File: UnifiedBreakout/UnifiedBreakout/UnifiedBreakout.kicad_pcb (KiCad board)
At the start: 2 copper layers, 15 parts, among them J1 MESA P3, J10 LIM Z, J11 ENCODER OUT, J12 PENDANT, J2 MESA P2, J3 ENCODER IN, J4 LIM X, J5 MOT X, J6 MOT Y, J7 ATX-24, J8 MOT Z, J9 LIM Y, K1 MOTOR POWER, K2 MIST, K3 DRAWBAR

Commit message: Unified breakout schematic "done"
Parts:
- removed K1: MOTOR POWER, Relay_THT:Relay_DPDT_Finder_40.52
- removed K2: MIST, Relay_THT:Relay_DPDT_Finder_40.52
- removed K3: DRAWBAR, Relay_THT:Relay_DPDT_Finder_40.52
- added C1: 100n, Capacitor_THT:C_Rect_L7.0mm_W2.0mm_P5.00mm, F.Cu at (149.4, 68.6)
- added C2: 100uF, Capacitor_THT:CP_Radial_D6.3mm_P2.50mm, F.Cu at (166.9, 62.7)
- added C3: 100n, Capacitor_THT:C_Rect_L7.0mm_W2.0mm_P5.00mm, F.Cu at (166.2, 46.5)
- added C4: 100uF, Capacitor_THT:CP_Radial_D6.3mm_P2.50mm, F.Cu at (158.9, 67.2)
- added C5: 100n, Capacitor_THT:C_Rect_L7.0mm_W2.0mm_P5.00mm, F.Cu at (166.2, 50.0)
- added C6: 100uF, Capacitor_THT:CP_Radial_D6.3mm_P2.50mm, F.Cu at (190.7, 44.2)
- added C7: 100n, Capacitor_THT:C_Rect_L7.0mm_W2.0mm_P5.00mm, F.Cu at (149.4, 65.0)
- added C8: 100uF, Capacitor_THT:CP_Radial_D6.3mm_P2.50mm, F.Cu at (177.0, 58.7)
- added D1: MESA P3 PWR, LED_THT:LED_D3.0mm, F.Cu at (189.6, 50.9)
- added D10: 1N4001, Diode_THT:D_DO-41_SOD81_P10.16mm_Horizontal, F.Cu at (178.1, 90.8)
- added D2: MESA P2 PWR, LED_THT:LED_D3.0mm, F.Cu at (173.8, 65.4)
- added D3: ATX PWR GOOD, LED_THT:LED_D3.0mm, F.Cu at (192.4, 35.9)
- added D4: ATX STBY, LED_THT:LED_D3.0mm, F.Cu at (192.4, 30.4)
- added D5: LED, LED_THT:LED_D3.0mm, F.Cu at (62.7, 177.5)
- added D6: 1N4001, Diode_THT:D_DO-41_SOD81_P10.16mm_Horizontal, F.Cu at (35.6, 176.9)
- added D7: LED, LED_THT:LED_D3.0mm, F.Cu at (121.2, 143.2)
- added D8: 1N4001, Diode_THT:D_DO-41_SOD81_P10.16mm_Horizontal, F.Cu at (94.2, 142.6)
- added D9: LED, LED_THT:LED_D3.0mm, F.Cu at (205.1, 91.5)
- added J13: ENCODER IN, Connector_Dsub:DSUB-15_Female_Horizontal_P2.77x2.84mm_EdgePinOffset7.70mm_Housed_MountingHolesOffset9.12mm, F.Cu at (64.1, 30.9)
- added J14: ARGON J5, Connector_IDC:IDC-Header_2x13_P2.54mm_Vertical, F.Cu at (271.8, 103.6)
- added J15: ARGON J2.2, Connector_RJ:RJ45_Ninigi_GE, F.Cu at (265.0, 32.8)
- added J16: RJ14, Connector_RJ:RJ12_Amphenol_54601, F.Cu at (142.1, 128.9)
- added J17: RJ14, Connector_RJ:RJ12_Amphenol_54601, F.Cu at (181.8, 128.9)
- added J18: RJ14, Connector_RJ:RJ12_Amphenol_54601, F.Cu at (180.0, 152.6)
- added J19: RJ14, Connector_RJ:RJ12_Amphenol_54601, F.Cu at (269.4, 55.6)
- added J20: RJ14, Connector_RJ:RJ12_Amphenol_54601, F.Cu at (224.1, 113.5)
- added J21: PENDANT, Connector_Dsub:DSUB-25_Female_Horizontal_P2.77x2.84mm_EdgePinOffset7.70mm_Housed_MountingHolesOffset9.12mm, F.Cu at (84.3, 198.6)
- added J22: RJ14, Connector_RJ:RJ12_Amphenol_54601, F.Cu at (140.2, 155.0)
- added J23: RJ14, Connector_RJ:RJ12_Amphenol_54601, F.Cu at (226.0, 89.8)
- added JP1: ENCODER PWR SEL, Connector_PinHeader_2.54mm:PinHeader_1x03_P2.54mm_Vertical, F.Cu at (77.4, 29.9)
- added JP2: HSIN1, Connector_PinHeader_2.54mm:PinHeader_1x03_P2.54mm_Vertical, F.Cu at (46.8, 79.8)
- added JP3: HSIN2, Connector_PinHeader_2.54mm:PinHeader_1x03_P2.54mm_Vertical, F.Cu at (51.5, 79.8)
- added Q1: BC547, Package_TO_SOT_THT:TO-92_Inline_Wide, F.Cu at (65.6, 163.5)
- added Q2: BC547, Package_TO_SOT_THT:TO-92_Inline_Wide, F.Cu at (124.1, 129.3)
- added Q3: BC547, Package_TO_SOT_THT:TO-92_Inline_Wide, F.Cu at (208.0, 77.5)
- added R1: 2K2, Resistor_THT:R_Axial_DIN0207_L6.3mm_D2.5mm_P10.16mm_Horizontal, F.Cu at (135.8, 57.2)
- added R10: 2K2, Resistor_THT:R_Axial_DIN0207_L6.3mm_D2.5mm_P10.16mm_Horizontal, F.Cu at (107.8, 142.5)
- added R11: 680R, Resistor_THT:R_Axial_DIN0207_L6.3mm_D2.5mm_P10.16mm_Horizontal, F.Cu at (93.9, 146.8)
- added R12: 2K2, Resistor_THT:R_Axial_DIN0207_L6.3mm_D2.5mm_P10.16mm_Horizontal, F.Cu at (177.8, 95.0)
- added R13: 680R, Resistor_THT:R_Axial_DIN0207_L6.3mm_D2.5mm_P10.16mm_Horizontal, F.Cu at (191.7, 90.7)
- added R14: 2K2, Resistor_THT:R_Axial_DIN0207_L6.3mm_D2.5mm_P10.16mm_Horizontal, F.Cu at (154.6, 128.7)
- added R15: 220K, Resistor_THT:R_Axial_DIN0207_L6.3mm_D2.5mm_P10.16mm_Horizontal, F.Cu at (154.6, 132.7)
- added R16: 2K2, Resistor_THT:R_Axial_DIN0207_L6.3mm_D2.5mm_P10.16mm_Horizontal, F.Cu at (194.3, 132.7)
- added R17: 220K, Resistor_THT:R_Axial_DIN0207_L6.3mm_D2.5mm_P10.16mm_Horizontal, F.Cu at (194.3, 128.7)
- added R18: 2K2, Resistor_THT:R_Axial_DIN0207_L6.3mm_D2.5mm_P10.16mm_Horizontal, F.Cu at (192.4, 156.4)
- added R19: 220K, Resistor_THT:R_Axial_DIN0207_L6.3mm_D2.5mm_P10.16mm_Horizontal, F.Cu at (192.4, 152.3)
- added R2: 220R, Resistor_THT:R_Axial_DIN0207_L6.3mm_D2.5mm_P10.16mm_Horizontal, F.Cu at (149.2, 61.2)
- added R20: 2K2, Resistor_THT:R_Axial_DIN0207_L6.3mm_D2.5mm_P10.16mm_Horizontal, F.Cu at (281.8, 59.4)
- added R21: 220K, Resistor_THT:R_Axial_DIN0207_L6.3mm_D2.5mm_P10.16mm_Horizontal, F.Cu at (281.8, 55.3)
- added R22: 2K2, Resistor_THT:R_Axial_DIN0207_L6.3mm_D2.5mm_P10.16mm_Horizontal, F.Cu at (236.6, 117.3)
- added R23: 220K, Resistor_THT:R_Axial_DIN0207_L6.3mm_D2.5mm_P10.16mm_Horizontal, F.Cu at (236.6, 113.2)
- added R24: 2K2, Resistor_THT:R_Axial_DIN0207_L6.3mm_D2.5mm_P10.16mm_Horizontal, F.Cu at (152.7, 154.8)
- added R25: 220K, Resistor_THT:R_Axial_DIN0207_L6.3mm_D2.5mm_P10.16mm_Horizontal, F.Cu at (152.7, 158.8)
- added R26: 2K2, Resistor_THT:R_Axial_DIN0207_L6.3mm_D2.5mm_P10.16mm_Horizontal, F.Cu at (238.5, 89.6)
- added R27: 220K, Resistor_THT:R_Axial_DIN0207_L6.3mm_D2.5mm_P10.16mm_Horizontal, F.Cu at (238.5, 93.7)
- added R3: 220R, Resistor_THT:R_Axial_DIN0207_L6.3mm_D2.5mm_P10.16mm_Horizontal, F.Cu at (162.5, 56.8)
- added R4: 220R, Resistor_THT:R_Axial_DIN0207_L6.3mm_D2.5mm_P10.16mm_Horizontal, F.Cu at (149.2, 57.2)
- added R5: 220R, Resistor_THT:R_Axial_DIN0207_L6.3mm_D2.5mm_P10.16mm_Horizontal, F.Cu at (135.8, 61.2)
- added R6: 220K, Resistor_THT:R_Axial_DIN0207_L6.3mm_D2.5mm_P10.16mm_Horizontal, F.Cu at (155.1, 42.7)
- added R7: 2K2, Resistor_THT:R_Axial_DIN0207_L6.3mm_D2.5mm_P10.16mm_Horizontal, F.Cu at (135.8, 65.3)
- added R8: 2K2, Resistor_THT:R_Axial_DIN0207_L6.3mm_D2.5mm_P10.16mm_Horizontal, F.Cu at (49.2, 176.8)
- added R9: 680R, Resistor_THT:R_Axial_DIN0207_L6.3mm_D2.5mm_P10.16mm_Horizontal, F.Cu at (35.3, 181.0)
- added RL1: JW2, Relay_THT:Relay_DPDT_Panasonic_JW2, F.Cu at (37.0, 171.2)
- added RL2: JW2, Relay_THT:Relay_DPDT_Panasonic_JW2, F.Cu at (95.5, 136.9)
- added RL3: JW2, Relay_THT:Relay_DPDT_Panasonic_JW2, F.Cu at (179.4, 85.1)
- added U1: 4N35, Package_DIP:DIP-6_W7.62mm, F.Cu at (155.2, 46.8)
- added U2: 4N35, Package_DIP:DIP-6_W7.62mm, F.Cu at (154.7, 136.8)
- added U3: 4N35, Package_DIP:DIP-6_W7.62mm, F.Cu at (194.4, 136.8)
- added U4: 4N35, Package_DIP:DIP-6_W7.62mm, F.Cu at (192.5, 160.5)
- added U5: 4N35, Package_DIP:DIP-6_W7.62mm, F.Cu at (281.9, 63.5)
- added U6: 4N35, Package_DIP:DIP-6_W7.62mm, F.Cu at (236.7, 121.4)
- added U7: 4N35, Package_DIP:DIP-6_W7.62mm, F.Cu at (152.8, 162.9)
- added U8: 4N35, Package_DIP:DIP-6_W7.62mm, F.Cu at (238.6, 97.8)
- J1: value MESA P3 -> 24V DC; footprint Connector_Dsub:DSUB-25_Female_Horizontal_P2.77x2.84mm_EdgePinOffset4.94mm_Housed_MountingHolesOffset7.48mm -> Connector_BarrelJack:BarrelJack_Horizontal
- J10: value LIM Z -> MESA P2 INTERNAL IO; footprint Connector_RJ:RJ12_Amphenol_54601 -> Connector_Dsub:DSUB-25_Female_Horizontal_P2.77x2.84mm_EdgePinOffset7.70mm_Housed_MountingHolesOffset9.12mm
- J11: value ENCODER OUT -> MESA P3 REAR IO; footprint Connector_Dsub:DSUB-15_Female_Horizontal_P2.77x2.84mm_EdgePinOffset4.94mm_Housed_MountingHolesOffset7.48mm -> Connector_Dsub:DSUB-25_Female_Horizontal_P2.77x2.84mm_EdgePinOffset7.70mm_Housed_MountingHolesOffset9.12mm
- J12: value PENDANT -> ENCODER OUT; footprint Connector_Dsub:DSUB-25_Female_Horizontal_P2.77x2.84mm_EdgePinOffset4.94mm_Housed_MountingHolesOffset7.48mm -> Connector_Dsub:DSUB-15_Female_Horizontal_P2.77x2.84mm_EdgePinOffset7.70mm_Housed_MountingHolesOffset9.12mm
- J2: value MESA P2 -> ATX-24; footprint Connector_Dsub:DSUB-25_Female_Horizontal_P2.77x2.84mm_EdgePinOffset4.94mm_Housed_MountingHolesOffset7.48mm -> Connector_Molex:Molex_Mini-Fit_Jr_5566-24A_2x12_P4.20mm_Vertical
- J3: value ENCODER IN -> 5V BUS; footprint Connector_RJ:RJ45_Amphenol_54602-x08_Horizontal -> Connector_Phoenix_MSTB:PhoenixContact_MSTBA_2,5_2-G-5,08_1x02_P5.08mm_Horizontal
- J4: value LIM X -> 24V BUS; footprint Connector_RJ:RJ12_Amphenol_54601 -> Connector_Phoenix_MSTB:PhoenixContact_MSTBA_2,5_2-G-5,08_1x02_P5.08mm_Horizontal
- J5: value MOT X -> 12V BUS; footprint Connector_RJ:RJ45_Amphenol_54602-x08_Horizontal -> Connector_Phoenix_MSTB:PhoenixContact_MSTBA_2,5_2-G-5,08_1x02_P5.08mm_Horizontal
- J6: value MOT Y -> ARGON RS485; footprint Connector_RJ:RJ45_Amphenol_54602-x08_Horizontal -> Connector_Phoenix_MSTB:PhoenixContact_MSTBA_2,5_3-G-5,08_1x03_P5.08mm_Horizontal
- J7: value ATX-24 -> RJ45; footprint Connector_Molex:Molex_Mini-Fit_Jr_5566-24A_2x12_P4.20mm_Vertical -> Connector_RJ:RJ45_Ninigi_GE
- J8: value MOT Z -> RJ45; footprint Connector_RJ:RJ45_Amphenol_54602-x08_Horizontal -> Connector_RJ:RJ45_Ninigi_GE
- J9: value LIM Y -> RJ45; footprint Connector_RJ:RJ12_Amphenol_54601 -> Connector_RJ:RJ45_Ninigi_GE
- moved J10 142.5 mm to (140.2, 197.8)
- moved J11 137.8 mm to (199.6, 198.6)
- moved J12 118.9 mm to (64.1, 52.4)
- moved J7 75.9 mm to (98.2, 158.0)
- moved J5 74.9 mm to (178.3, 43.7)
- moved J8 68.5 mm to (227.3, 67.1)
- moved J6 66.3 mm to (124.6, 44.1)
- moved J1 61.8 mm to (188.2, 33.0)
- moved J9 47.3 mm to (182.1, 106.2)
- moved J3 42.4 mm to (143.9, 44.1)
- moved J4 36.8 mm to (124.6, 58.6)
- moved J2 33.6 mm to (123.8, 30.9)
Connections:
- net Net-(J8-Pad5) renamed /Y MOT/ENABLE
- net Net-(J8-Pad7) renamed /Y MOT/ALARM
- net Net-(J9-Pad5) renamed /Z MOT/ENABLE
- J1 pad 1: Net-(J1-Pad1) -> +24V
- J1 pad 2: Net-(J1-Pad2) -> GND
- J10 pad 1: Net-(J10-Pad1) -> /AXIS_PWR
- J10 pad 2: Net-(J10-Pad2) -> /GPI1
- J10 pad 3: Net-(J10-Pad3) -> /GPI2
- J10 pad 4: Net-(J10-Pad4) -> /PENDANT_MULX100
- J10 pad 5: Net-(J10-Pad5) -> /PENDANT_MULX10
- J10 pad 6: Net-(J10-Pad6) -> /PENDANT_MULX1
- J11 pad 0: Net-(J11-Pad0) -> GND
- J11 pad 1: Net-(J11-Pad1) -> /ESTOP
- J11 pad 10: Net-(J11-Pad10) -> /LIMIT_Z
- J11 pad 11: Net-(J11-Pad11) -> /SPINDLE_ENC_A
- J11 pad 12: Net-(J11-Pad12) -> /SPINDLE_ENC_B
- J11 pad 13: Net-(J11-Pad13) -> /SPINDLE_ENC_IDX
- J11 pad 14: Net-(J11-Pad14) -> /SPINDLE_PWM_SIG
- J11 pad 15: Net-(J11-Pad15) -> /LIMIT_X
- J11 pad 2: Net-(J11-Pad2) -> /MESA P3 REAR IO/IO_02_STEPGEN_00_STEP
- J11 pad 3: Net-(J11-Pad3) -> /X MOT/DIR
- J11 pad 4: Net-(J11-Pad4) -> /MESA P3 REAR IO/IO_06_STEPGEN_01_STEP
- J11 pad 5: Net-(J11-Pad5) -> /Y MOT/DIR
- J11 pad 6: Net-(J11-Pad6) -> /MESA P3 REAR IO/IO_09_STEPGEN_02_STEP
- J11 pad 7: Net-(J11-Pad7) -> /Z MOT/DIR
- J11 pad 8: Net-(J11-Pad8) -> /SPINDLE_STEPGEN_STEP
- J11 pad 9: Net-(J11-Pad9) -> /SPINDLE_STEPGEN_DIR
- J12 pad 0: Net-(J12-Pad0) -> GND
- J12 pad 14: Net-(J12-Pad14) -> /ARGON ENCODER/IDX-
- J12 pad 15: Net-(J12-Pad15) -> /SPINDLE_ENC_IDX
- J12 pad 5: Net-(J12-Pad5) -> /ARGON ENCODER/B-
- J12 pad 6: Net-(J12-Pad6) -> /SPINDLE_ENC_B
- J12 pad 7: Net-(J12-Pad7) -> /ARGON ENCODER/A-
- J12 pad 8: Net-(J12-Pad8) -> /SPINDLE_ENC_A
- J2 pad 10: Net-(J2-Pad10) -> +12V
- J2 pad 11: Net-(J2-Pad11) -> +12V
- J2 pad 12: Net-(J2-Pad12) -> Net-(J2-Pad1)
- J2 pad 13: Net-(J2-Pad13) -> Net-(J2-Pad1)
- J2 pad 15: Net-(J2-Pad15) -> GND
- J2 pad 17: Net-(J2-Pad17) -> GND
- J2 pad 18: Net-(J2-Pad18) -> GND
- J2 pad 19: Net-(J2-Pad19) -> GND
- J2 pad 2: Net-(J2-Pad2) -> Net-(J2-Pad1)
- J2 pad 21: Net-(J2-Pad21) -> +5V
- J2 pad 22: Net-(J2-Pad22) -> +5V
- J2 pad 23: Net-(J2-Pad23) -> +5V
- J2 pad 24: Net-(J2-Pad24) -> GND
- J2 pad 3: Net-(J2-Pad3) -> GND
- J2 pad 4: Net-(J2-Pad4) -> +5V
- J2 pad 5: Net-(J2-Pad5) -> GND
- J2 pad 6: Net-(J2-Pad6) -> +5V
- J2 pad 7: Net-(J2-Pad7) -> GND
- J3 pad 1: Net-(J3-Pad1) -> +5V
- J3 pad 2: Net-(J3-Pad2) -> GND
- J4 pad 1: Net-(J4-Pad1) -> +24V
- J4 pad 2: Net-(J4-Pad2) -> GND
- J5 pad 1: Net-(J5-Pad1) -> +12V
- J5 pad 2: Net-(J5-Pad2) -> GND
- J6 pad 1: Net-(J6-Pad1) -> /ARGON ESTOP/RS485_A
- J6 pad 2: Net-(J6-Pad2) -> /ARGON ESTOP/RS485_B
- J6 pad 3: Net-(J6-Pad3) -> GND
- J7 pad 1: Net-(J7-Pad1) -> /MESA P3 REAR IO/IO_02_STEPGEN_00_STEP
- J7 pad 2: Net-(J7-Pad1) -> GND
- J7 pad 3: Net-(J7-Pad15) -> /X MOT/DIR
- J7 pad 4: Net-(J7-Pad21) -> GND
- J7 pad 5: Net-(J7-Pad15) -> /X MOT/ENABLE
- J7 pad 6: Net-(J7-Pad21) -> GND
- J7 pad 7: Net-(J7-Pad15) -> /X MOT/ALARM
- J7 pad 8: Net-(J7-Pad8) -> GND
- J7 pad 9: Net-(J7-Pad9) -> (no net)
- J8 pad 1: Net-(J8-Pad1) -> /MESA P3 REAR IO/IO_06_STEPGEN_01_STEP
- J8 pad 2: Net-(J8-Pad2) -> GND
- J8 pad 3: Net-(J8-Pad3) -> /Y MOT/DIR
- J8 pad 4: Net-(J8-Pad4) -> GND
- J8 pad 6: Net-(J8-Pad6) -> GND
- J8 pad 8: Net-(J8-Pad8) -> GND
- J9 pad 1: Net-(J9-Pad1) -> /MESA P3 REAR IO/IO_09_STEPGEN_02_STEP
- J9 pad 2: Net-(J9-Pad2) -> GND
- J9 pad 3: Net-(J9-Pad3) -> /Z MOT/DIR
- J9 pad 4: Net-(J9-Pad4) -> GND
- J9 pad 6: Net-(J9-Pad6) -> GND
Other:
- rule pad_to_mask_clearance: 0.051 -> 0

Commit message: Invert outputs for active low, other cleanup
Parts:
- removed J22, J23: RJ14, Connector_RJ:RJ12_Amphenol_54601
- removed R27: 220K, Resistor_THT:R_Axial_DIN0207_L6.3mm_D2.5mm_P10.16mm_Horizontal
- removed U8: 4N35, Package_DIP:DIP-6_W7.62mm
- J14: footprint Connector_IDC:IDC-Header_2x13_P2.54mm_Vertical -> Connector_IDC:IDC-Header_2x13_P2.54mm_Horizontal
- J2: footprint Connector_Molex:Molex_Mini-Fit_Jr_5566-24A_2x12_P4.20mm_Vertical -> Connector_Molex:Molex_Mini-Fit_Jr_5569-24A2_2x12_P4.20mm_Horizontal
- R24, R26: value 2K2 -> 10K
- R25: value 220K -> 10K
- U7: value 4N35 -> 74HC14; footprint Package_DIP:DIP-6_W7.62mm -> Package_DIP:DIP-14_W7.62mm_LongPads
- moved J10 203.4 mm to (255.8, 30.5)
- moved J14 156.5 mm to (131.9, 33.3)
- moved C3 140.7 mm to (43.2, 114.8)
- moved R26 138.5 mm to (100.0, 93.5)
- moved J1 135.9 mm to (67.5, 95.4)
- moved U7 130.3 mm to (43.4, 92.2)
- moved R3 123.7 mm to (56.3, 120.2)
- moved J11 121.6 mm to (171.3, 80.3)
- moved R21 120.8 mm to (190.3, 134.2)
- moved D3 120.3 mm to (103.5, 116.9)
- moved U5 118.2 mm to (190.4, 138.3)
- moved J19 118.2 mm to (177.8, 130.4)
- moved D4 116.0 mm to (109.4, 111.3)
- moved R20 115.7 mm to (190.3, 130.2)
- moved C1 114.4 mm to (43.2, 111.3)
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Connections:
- net /ARGON IO/GPI1 renamed Net-(J14-Pad20)
- net /ARGON IO/GPI2 renamed Net-(J14-Pad22)
- net /ARGON IO/GPI3 renamed Net-(J14-Pad24)
- net /ARGON IO/GPI4 renamed Net-(J14-Pad26)
- net /ARGON IO/GPO1 renamed Net-(J14-Pad12)
- net /ARGON IO/GPO2 renamed Net-(J14-Pad14)
- net /ARGON IO/GPO4 renamed Net-(J14-Pad18)
- J10 pad 2: /GPI1 -> /ALARM
- J10 pad 3: /GPI2 -> /ATX_PWR
- J14 pad 15: Net-(J14-Pad15) -> GND
- J14 pad 16: /ARGON IO/GPO3 -> /ALARM
- J2 pad 16: Net-(J2-Pad16) -> /ATX_PWR
- J7 pad 7: /X MOT/ALARM -> /ALARM
- J8 pad 7: /Y MOT/ALARM -> /ALARM
- J9 pad 7: /Z MOT/ALARM -> /ALARM
- R1 pad 2: Net-(J2-Pad16) -> /ATX_PWR
- R10 pad 2: /DRAWBAR_VALVE -> /DRAWBAR RELAY/ENABLE
- R12 pad 2: /MIST -> /MIST RELAY/ENABLE
- R24 pad 1: Net-(R24-Pad1) -> +5VP
- R24 pad 2: GND -> /AXIS_PWR
- R25 pad 1: Net-(R25-Pad1) -> +5VP
- R25 pad 2: GND -> /DRAWBAR_VALVE
- R26 pad 1: Net-(R26-Pad1) -> +5VP
- R26 pad 2: GND -> /MIST
- R8 pad 2: /AXIS_PWR -> /AXIS POWER RELAY/ENABLE
- U7 pad 1: Net-(J22-Pad3) -> /AXIS_PWR
- U7 pad 2: Net-(R24-Pad1) -> /AXIS POWER RELAY/ENABLE
- U7 pad 3: Net-(U7-Pad3) -> /DRAWBAR_VALVE
- U7 pad 4: GND -> /DRAWBAR RELAY/ENABLE
- U7 pad 5: /GPI1 -> /MIST
- U7 pad 6: Net-(R25-Pad1) -> /MIST RELAY/ENABLE

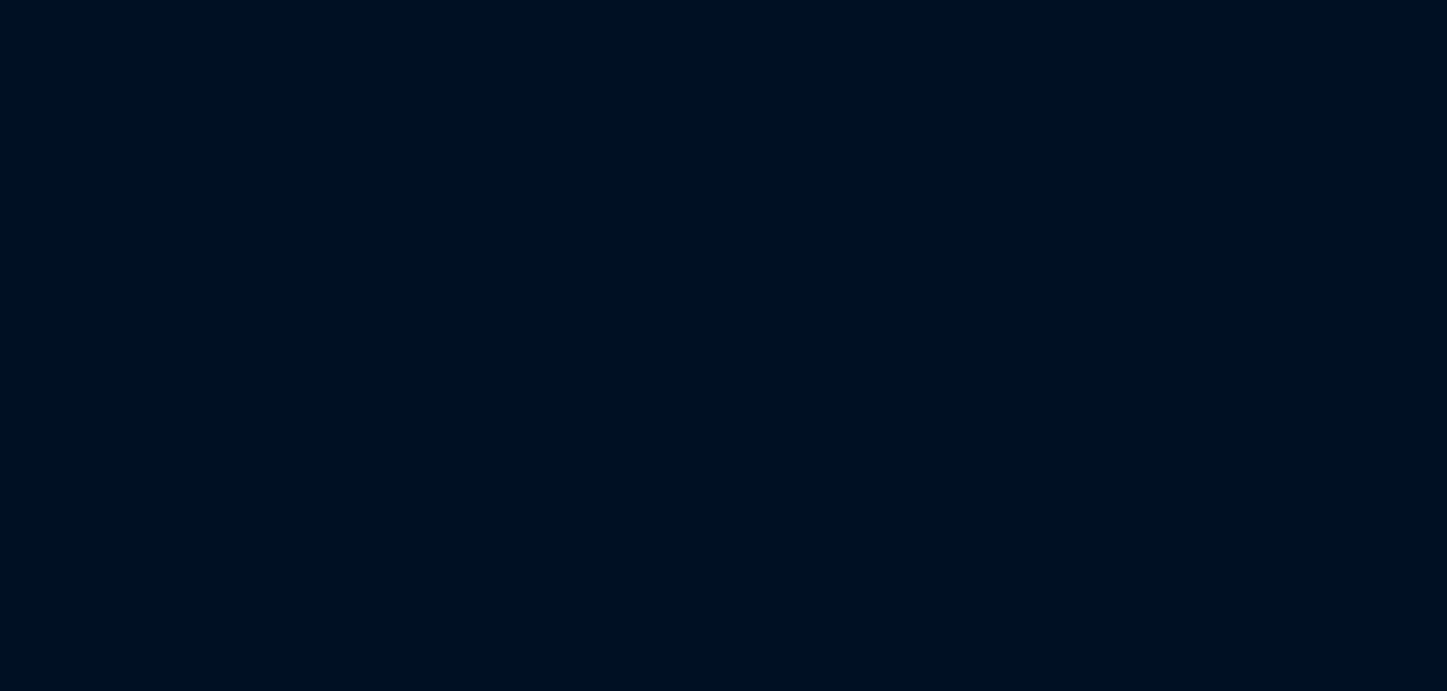
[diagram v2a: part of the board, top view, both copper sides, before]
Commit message: Add extra pullups on inputs
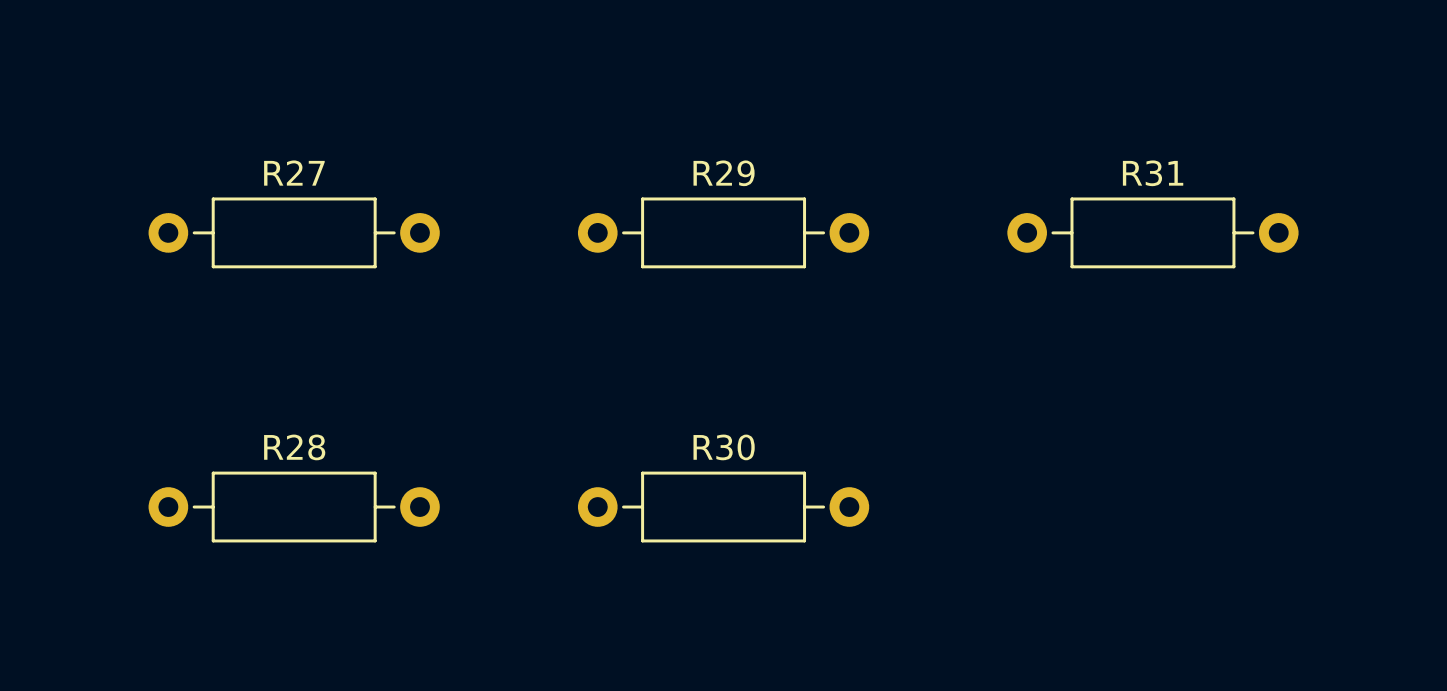
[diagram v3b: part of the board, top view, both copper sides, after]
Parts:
- added R27: 10K, Resistor_THT:R_Axial_DIN0207_L6.3mm_D2.5mm_P10.16mm_Horizontal, F.Cu at (224.5, 141.2)
- added R28: 10K, Resistor_THT:R_Axial_DIN0207_L6.3mm_D2.5mm_P10.16mm_Horizontal, F.Cu at (224.5, 152.3)
- added R29: 10K, Resistor_THT:R_Axial_DIN0207_L6.3mm_D2.5mm_P10.16mm_Horizontal, F.Cu at (241.9, 141.2)
- added R30: 10K, Resistor_THT:R_Axial_DIN0207_L6.3mm_D2.5mm_P10.16mm_Horizontal, F.Cu at (241.9, 152.3)
- added R31: 10K, Resistor_THT:R_Axial_DIN0207_L6.3mm_D2.5mm_P10.16mm_Horizontal, F.Cu at (259.2, 141.2)

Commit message: Connectors placed
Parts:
- added H1: MountingHole, MountingHole:MountingHole_3.2mm_M3, F.Cu at (-4.45, 19.1)
- added H2: MountingHole, MountingHole:MountingHole_3.2mm_M3, F.Cu at (-2.54, 221.0)
- added H3: MountingHole, MountingHole:MountingHole_3.2mm_M3, F.Cu at (217.2, 76.8)
- added H4: MountingHole, MountingHole:MountingHole_3.2mm_M3, F.Cu at (196.2, 221.0)
- added J22: DRAWBAR, Connector_Phoenix_MSTB:PhoenixContact_MSTBA_2,5_2-G-5,08_1x02_P5.08mm_Horizontal, F.Cu at (167.5, 21.3)
- added J23: MIST, Connector_Phoenix_MSTB:PhoenixContact_MSTBA_2,5_2-G-5,08_1x02_P5.08mm_Horizontal, F.Cu at (148.8, 21.3)
- added J24: AXIS PWR IN, Connector_Phoenix_MSTB:PhoenixContact_MSTBA_2,5_3-G-5,08_1x03_P5.08mm_Horizontal, F.Cu at (197.4, 21.3)
- added J25: AXIS PWR OUT, Connector_Phoenix_MSTB:PhoenixContact_MSTBA_2,5_3-G-5,08_1x03_P5.08mm_Horizontal, F.Cu at (221.7, 21.3)
- J1: value 24V DC -> 24V DC IN
- J16, J17, J18, J19, J20: footprint Connector_RJ:RJ12_Amphenol_54601 -> Connector_RJ:RJ14_Connfly_DS1133-S4_Horizontal
- moved J16 243.4 mm to (-5.59, 97.5), turned to 90 degrees
- moved J18 242.5 mm to (-5.59, 113.3), turned to 90 degrees
- moved J10 234.4 mm to (113.7, 216.9)
- moved J15 215.2 mm to (61.0, 25.9), turned to 180 degrees
- moved RL1 208.7 mm to (222.6, 62.9), turned to 90 degrees
- moved J8 204.2 mm to (0.51, 179.8), turned to 270 degrees
- moved J20 183.7 mm to (-5.59, 144.8), turned to 90 degrees
- moved J19 183.4 mm to (-5.59, 129.0), turned to 90 degrees
- moved J11 178.8 mm to (55.9, 216.9)
- moved J3 171.8 mm to (214.8, 194.3), turned to 90 degrees
- moved J4 168.1 mm to (214.8, 165.9), turned to 90 degrees
- moved J2 165.9 mm to (210.7, 90.5), turned to 270 degrees
- moved J17 163.5 mm to (-5.59, 81.8), turned to 90 degrees
- moved J1 153.2 mm to (211.2, 148.6), turned to 180 degrees
- moved J5 152.0 mm to (214.8, 180.1), turned to 90 degrees
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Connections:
- RL1 pad 3: /AXIS POWER RELAY/OUT_A -> /L_OUT
- RL1 pad 4: /AXIS POWER RELAY/IN_A -> /L_IN
- RL1 pad 5: /AXIS POWER RELAY/IN_B -> /N_IN
- RL1 pad 6: /AXIS POWER RELAY/OUT_B -> /N_OUT
- RL2 pad 3: /DRAWBAR RELAY/OUT_A -> GND
- RL3 pad 3: /MIST RELAY/OUT_A -> GND
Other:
- board outline added: 239.4 x 216.5 mm
- net class High power added: clearance 0.5, trace_width 1.5, via_dia 0.8, via_drill 0.4
- net class Low power added: clearance 0.5, trace_width 1, via_dia 0.8, via_drill 0.4
- net class Mains added: clearance 2.5, trace_width 3, via_dia 0.8, via_drill 0.4
- board text added: "DRAWBAR"
- board text added: "L"
- board text added: "LIMIT X"
- board text added: "LIMIT Y"
- board text added: "LIMIT Z"
- board text added: "N"
- board text added: "PE"
- board text added: "PROBE"
- board text added: "X AXIS"
- board text added: "Y AXIS"
- board text added: "Z AXIS"

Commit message: Did some more layout
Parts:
- moved R8 197.6 mm to (212.7, 55.9)
- moved D6 197.3 mm to (209.6, 71.1), turned to 180 degrees
- moved R9 195.9 mm to (208.9, 77.5), turned to 180 degrees
- moved D5 180.3 mm to (214.0, 69.2)
- moved Q1 173.7 mm to (215.3, 64.1)
- moved C1 171.6 mm to (193.0, 194.9), turned to 90 degrees
- moved C3 158.7 mm to (193.0, 166.9), turned to 90 degrees
- moved C2 129.4 mm to (201.9, 193.0), turned to 90 degrees
- moved C5 127.8 mm to (193.0, 180.9), turned to 90 degrees
- moved R3 123.7 mm to (128.9, 220.3), turned to 90 degrees
- moved C6 118.4 mm to (201.9, 179.1), turned to 90 degrees
- moved C4 117.4 mm to (201.9, 165.7), turned to 90 degrees
- moved C7 113.7 mm to (74.3, 212.1), turned to 90 degrees
- moved D1 107.1 mm to (62.2, 210.2)
- moved D2 106.7 mm to (120.0, 210.2)
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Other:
- net class Default: trace_width 0.25 -> 0.35
- net class Gnd added: clearance 0.2, trace_width 0.5, via_dia 0.8, via_drill 0.4

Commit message: More placement, add some custom parts
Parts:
- J1: footprint Connector_BarrelJack:BarrelJack_Horizontal -> SwitchCraft-BarrelJack-RAPC722BK:RAPC722BK
- J12: value ENCODER OUT -> ENCODER IN
- J13: value ENCODER IN -> ENCODER OUT
- J15, J7, J8, J9: footprint Connector_RJ:RJ45_Ninigi_GE -> Stewart:SS6488SANF1
- J16, J17, J18, J19, J20: footprint Connector_RJ:RJ14_Connfly_DS1133-S4_Horizontal -> Wurth:615004141121
- moved U3 165.7 mm to (13.7, 75.6)
- moved R16 155.7 mm to (13.7, 85.3)
- moved R17 152.9 mm to (26.9, 75.2), turned to 270 degrees
- moved R15 137.2 mm to (26.9, 91.2), turned to 270 degrees
- moved U6 122.3 mm to (13.8, 138.8)
- moved R18 121.9 mm to (13.7, 116.8)
- moved U5 120.5 mm to (13.7, 122.7)
- moved U2 119.2 mm to (13.8, 91.4)
- moved R22 119.0 mm to (14.0, 148.8)
- moved R20 117.9 mm to (13.7, 132.6)
- moved U4 116.0 mm to (13.7, 106.9)
- moved R14 107.8 mm to (13.7, 101.3)
- moved R19 107.4 mm to (26.9, 106.7), turned to 270 degrees
- moved R23 107.3 mm to (27.2, 138.7), turned to 270 degrees
- moved R21 106.8 mm to (26.9, 122.4), turned to 270 degrees
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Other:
- board text added: "ARGON"
- board text added: "MESA"
- board text added: "PWM"
- board text added: "SPINDLE SOURCE"
- board text added: "STEPGEN"

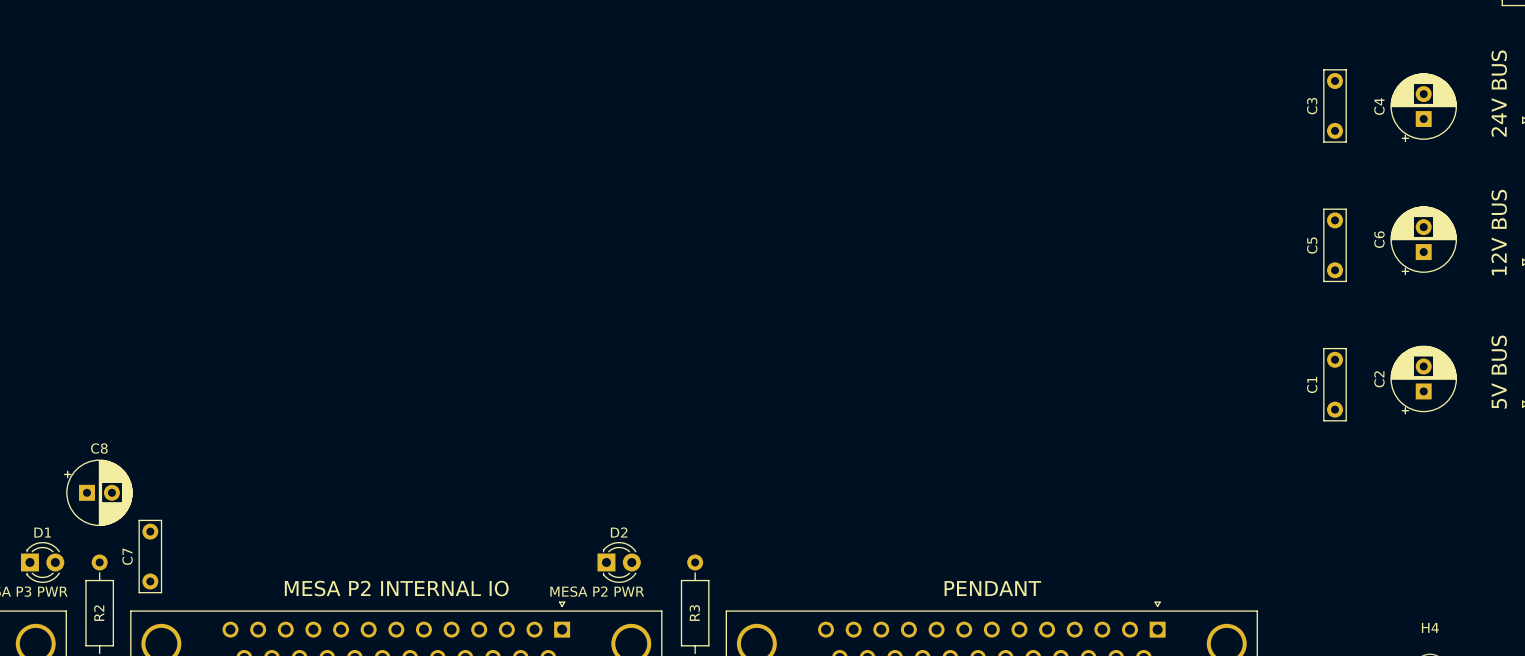
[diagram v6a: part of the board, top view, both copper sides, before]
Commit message: Assigned some parts
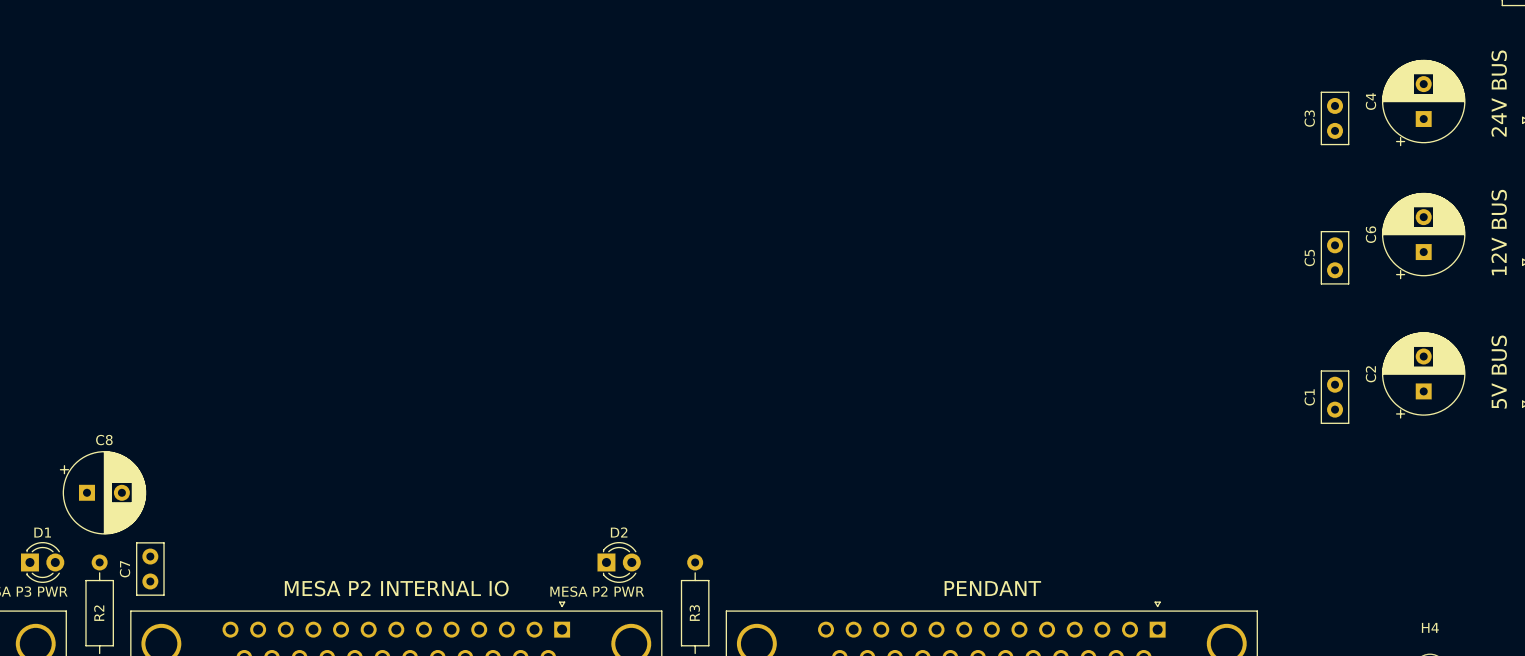
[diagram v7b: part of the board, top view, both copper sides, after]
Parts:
- C1, C3, C5, C7: footprint Capacitor_THT:C_Rect_L7.0mm_W2.0mm_P5.00mm -> Capacitor_THT:C_Disc_D5.0mm_W2.5mm_P2.50mm
- C2, C4, C6, C8: footprint Capacitor_THT:CP_Radial_D6.3mm_P2.50mm -> Capacitor_THT:CP_Radial_D8.0mm_P3.50mm
